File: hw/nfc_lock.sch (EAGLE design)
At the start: 2 parts, among them IC1 STM8S003F3, U1 M24SR16-YMN6T/2

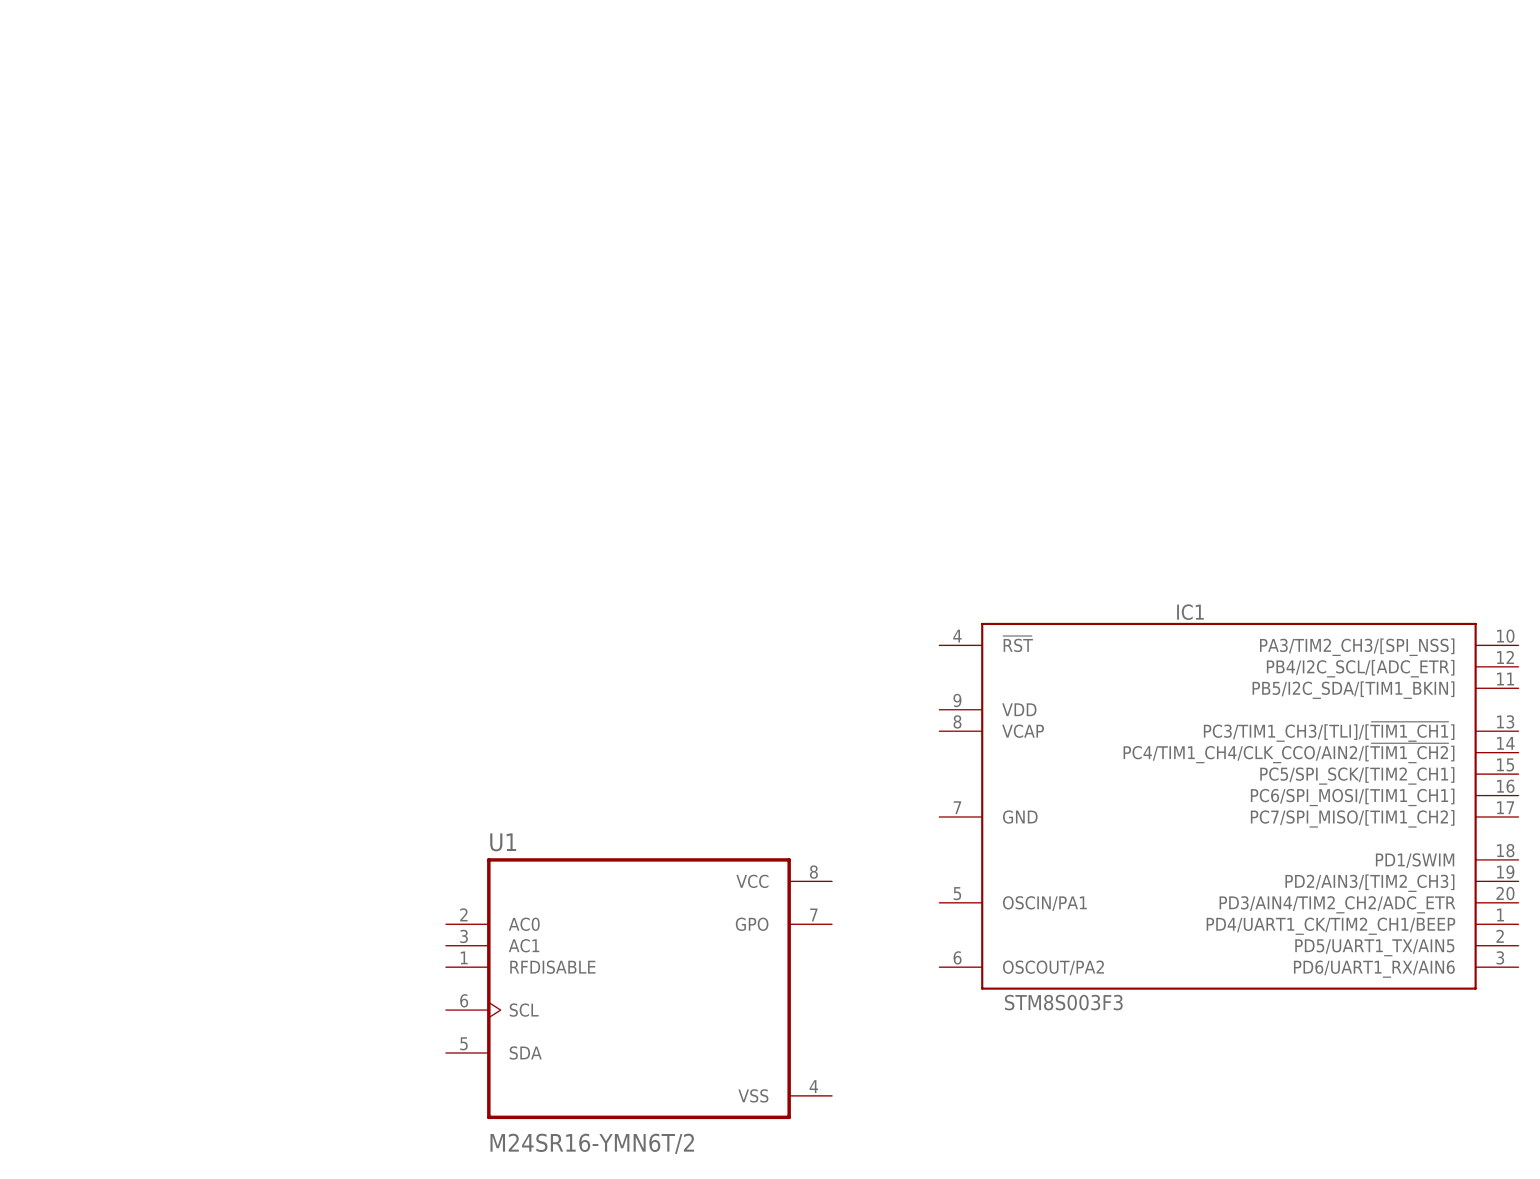
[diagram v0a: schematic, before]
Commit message: 3.3 voltage regulators + I2C lines
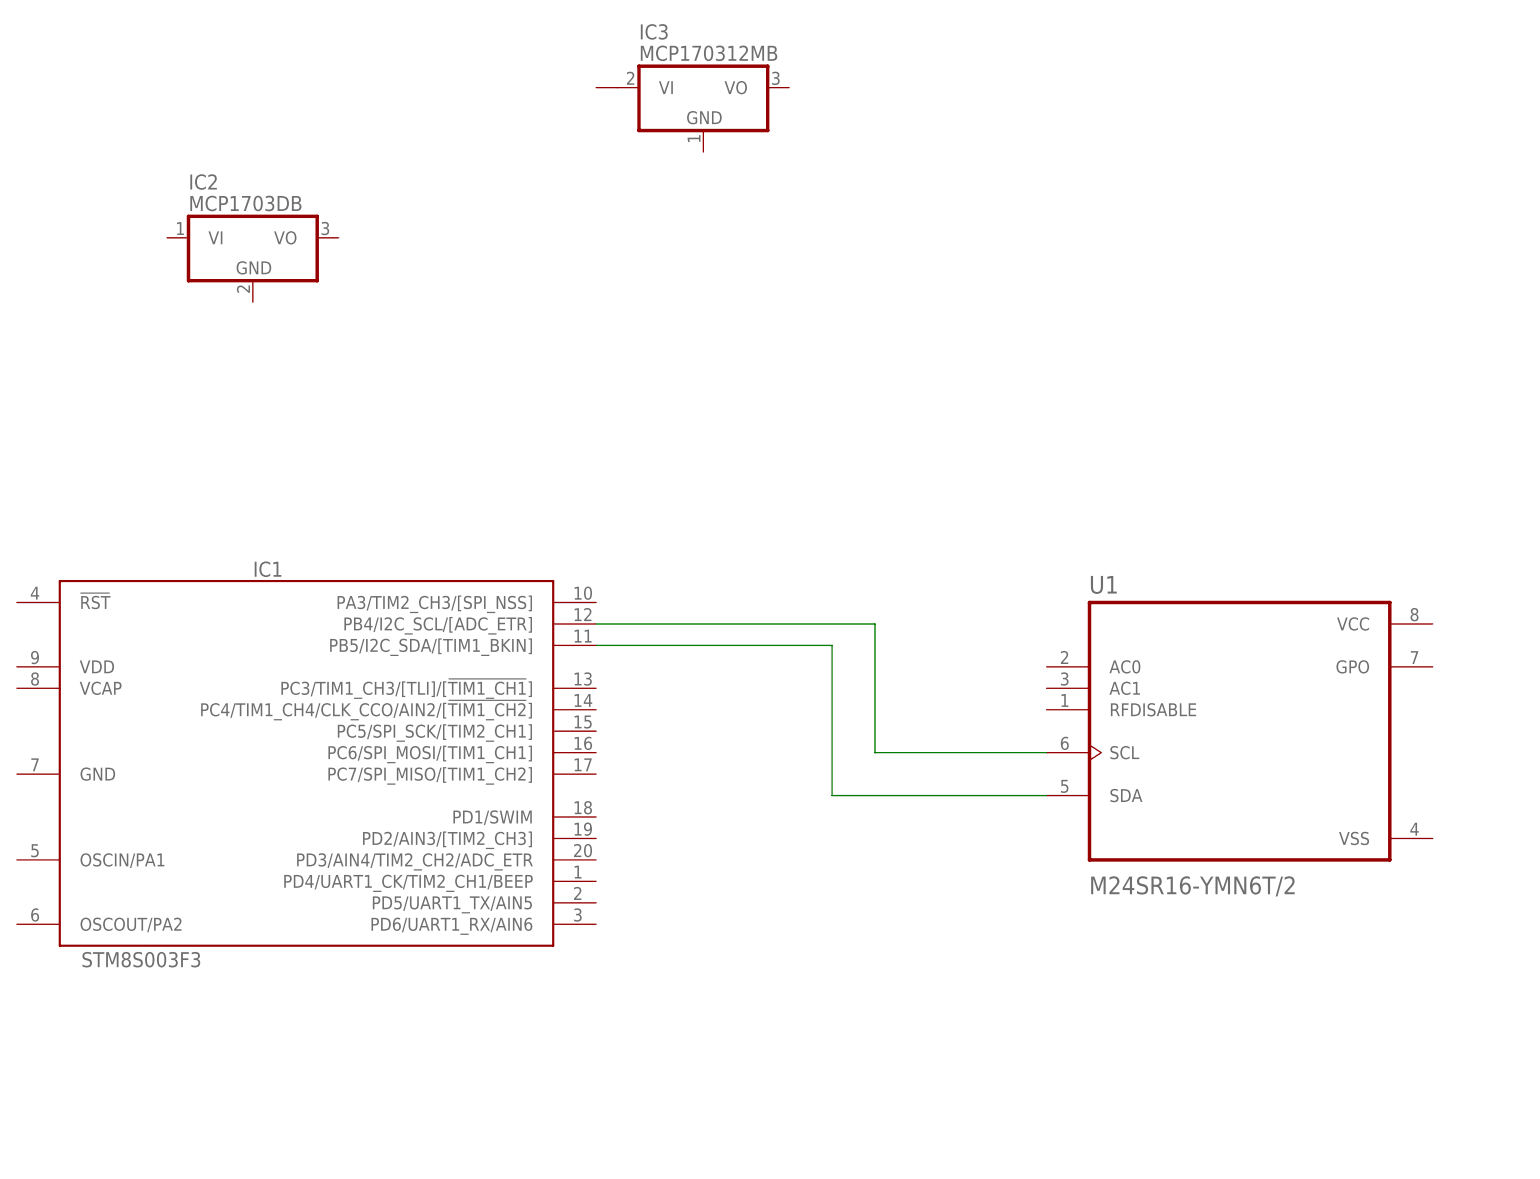
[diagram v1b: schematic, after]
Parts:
- added IC2: MCP1703DB, linear:MCP1703DB
- added IC3: MCP170312MB, linear:MCP170312MB
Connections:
- new net N$1: IC1.PB4/I2C_SCL/[ADC_ETR], U1.SCL
- new net N$2: IC1.PB5/I2C_SDA/[TIM1_BKIN], U1.SDA
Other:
- moved on the sheet: IC1, U1
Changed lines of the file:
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@@
 <part name="U1" library="m24sr16-ymn6t_2" deviceset="M24SR16-YMN6T/2" device=""/>
 <part name="IC1" library="stm8" deviceset="STM8S003" device="F3"/>
+<part name="IC2" library="linear" deviceset="MCP1703" device="DB"/>
+<part name="IC3" library="linear" deviceset="MCP1703*" device="MB" technology="12"/>
 </parts>
 <sheets>
@@
 </plain>
 <instances>
-<instance part="U1" gate="G$1" x="63.5" y="48.26"/>
-<instance part="IC1" gate="G$1" x="132.08" y="71.12"/>
+<instance part="U1" gate="G$1" x="134.62" y="78.74"/>
+<instance part="IC1" gate="G$1" x="22.86" y="76.2"/>
+<instance part="IC2" gate="G$1" x="17.78" y="137.16"/>
+<instance part="IC3" gate="G$1" x="71.12" y="154.94"/>
 </instances>
 <busses>
 </busses>
 <nets>
+<net name="N$1" class="0">
+<segment>
+<pinref part="IC1" gate="G$1" pin="PB4/I2C_SCL/[ADC_ETR]"/>
+<wire x1="58.42" y1="91.44" x2="91.44" y2="91.44" width="0.1524" layer="91"/>
+<wire x1="91.44" y1="91.44" x2="91.44" y2="76.2" width="0.1524" layer="91"/>
+<pinref part="U1" gate="G$1" pin="SCL"/>
+<wire x1="91.44" y1="76.2" x2="111.76" y2="76.2" width="0.1524" layer="91"/>
+</segment>
+</net>
+<net name="N$2" class="0">
+<segment>
+<pinref part="IC1" gate="G$1" pin="PB5/I2C_SDA/[TIM1_BKIN]"/>
+<wire x1="58.42" y1="88.9" x2="86.36" y2="88.9" width="0.1524" layer="91"/>
+<wire x1="86.36" y1="88.9" x2="86.36" y2="71.12" width="0.1524" layer="91"/>
+<pinref part="U1" gate="G$1" pin="SDA"/>
+<wire x1="86.36" y1="71.12" x2="111.76" y2="71.12" width="0.1524" layer="91"/>
+</segment>
+</net>
 </nets>
 </sheet>

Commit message: power supply circut
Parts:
- removed IC2: MCP1703DB, linear:MCP1703DB
- added C2: (no value), rcl:CPOL-EU153CLV-0405
- added C3: (no value), rcl:C-EUC1206
- added D1, D2: GF1, diode:GF1
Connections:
- new net +5V: D1.A
- new net +5V/1: C3.1, IC3.VO
- new net 0V: C2.-, C3.2, IC3.GND
- new net N$3: D1.C, D2.A
- new net N$4: C2.+, D2.C, IC3.VI1
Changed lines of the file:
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@@
 <layer number="97" name="Info" color="7" fill="1" visible="yes" active="yes"/>
 <layer number="98" name="Guide" color="6" fill="1" visible="yes" active="yes"/>
+<layer number="99" name="SpiceOrder" color="5" fill="1" visible="yes" active="yes"/>
 </layers>
 <schematic xreflabel="%F%N/%S.%C%R" xrefpart="/%S.%C%R">
@@
 <part name="U1" library="m24sr16-ymn6t_2" deviceset="M24SR16-YMN6T/2" device=""/>
 <part name="IC1" library="stm8" deviceset="STM8S003" device="F3"/>
-<part name="IC2" library="linear" deviceset="MCP1703" device="DB"/>
 <part name="IC3" library="linear" deviceset="MCP1703*" device="MB" technology="12"/>
+<part name="SUPPLY1" library="supply2" deviceset="+5V" device=""/>
+<part name="SUPPLY2" library="supply2" deviceset="+5V/1" device="" value="+3.3V"/>
+<part name="SUPPLY3" library="supply2" deviceset="0V" device=""/>
+<part name="C2" library="rcl" deviceset="CPOL-EU" device="153CLV-0405"/>
+<part name="C3" library="rcl" deviceset="C-EU" device="C1206"/>
+<part name="D1" library="diode" deviceset="GF1" device=""/>
+<part name="D2" library="diode" deviceset="GF1" device=""/>
+<part name="SUPPLY4" library="supply2" deviceset="0V" device=""/>
+<part name="SUPPLY5" library="supply2" deviceset="0V" device=""/>
 </parts>
 <sheets>
@@
 <instance part="U1" gate="G$1" x="134.62" y="78.74"/>
 <instance part="IC1" gate="G$1" x="22.86" y="76.2"/>
-<instance part="IC2" gate="G$1" x="17.78" y="137.16"/>
 <instance part="IC3" gate="G$1" x="71.12" y="154.94"/>
+<instance part="SUPPLY1" gate="+5V" x="27.94" y="157.48"/>
+<instance part="SUPPLY2" gate="G$1" x="93.98" y="157.48"/>
+<instance part="SUPPLY3" gate="0V" x="71.12" y="139.7"/>
+<instance part="C2" gate="G$1" x="53.34" y="152.4"/>
+<instance part="C3" gate="G$1" x="86.36" y="152.4"/>
+<instance part="D1" gate="D" x="35.56" y="154.94"/>
+<instance part="D2" gate="D" x="45.72" y="154.94"/>
+<instance part="SUPPLY4" gate="0V" x="86.36" y="139.7"/>
+<instance part="SUPPLY5" gate="0V" x="53.34" y="139.7"/>
 </instances>
 <busses>
@@
 </segment>
 </net>
+<net name="0V" class="0">
+<segment>
+<pinref part="IC3" gate="G$1" pin="GND"/>
+<pinref part="SUPPLY3" gate="0V" pin="0V"/>
+<wire x1="71.12" y1="142.24" x2="71.12" y2="147.32" width="0.1524" layer="91"/>
+</segment>
+<segment>
+<pinref part="C3" gate="G$1" pin="2"/>
+<pinref part="SUPPLY4" gate="0V" pin="0V"/>
+<wire x1="86.36" y1="142.24" x2="86.36" y2="147.32" width="0.1524" layer="91"/>
+</segment>
+<segment>
+<pinref part="C2" gate="G$1" pin="-"/>
+<pinref part="SUPPLY5" gate="0V" pin="0V"/>
+<wire x1="53.34" y1="142.24" x2="53.34" y2="147.32" width="0.1524" layer="91"/>
+</segment>
+</net>
+<net name="+5V/1" class="0">
+<segment>
+<pinref part="IC3" gate="G$1" pin="VO"/>
+<pinref part="SUPPLY2" gate="G$1" pin="+5V/1"/>
+<wire x1="93.98" y1="154.94" x2="86.36" y2="154.94" width="0.1524" layer="91"/>
+<pinref part="C3" gate="G$1" pin="1"/>
+<wire x1="86.36" y1="154.94" x2="81.28" y2="154.94" width="0.1524" layer="91"/>
+<junction x="86.36" y="154.94"/>
+</segment>
+</net>
+<net name="+5V" class="0">
+<segment>
+<pinref part="SUPPLY1" gate="+5V" pin="+5V"/>
+<pinref part="D1" gate="D" pin="A"/>
+<wire x1="33.02" y1="154.94" x2="27.94" y2="154.94" width="0.1524" layer="91"/>
+</segment>
+</net>
+<net name="N$3" class="0">
+<segment>
+<pinref part="D1" gate="D" pin="C"/>
+<pinref part="D2" gate="D" pin="A"/>
+<wire x1="43.18" y1="154.94" x2="38.1" y2="154.94" width="0.1524" layer="91"/>
+</segment>
+</net>
+<net name="N$4" class="0">
+<segment>
+<pinref part="IC3" gate="G$1" pin="VI1"/>
+<pinref part="D2" gate="D" pin="C"/>
+<wire x1="48.26" y1="154.94" x2="53.34" y2="154.94" width="0.1524" layer="91"/>
+<pinref part="C2" gate="G$1" pin="+"/>
+<wire x1="53.34" y1="154.94" x2="58.42" y2="154.94" width="0.1524" layer="91"/>
+<junction x="53.34" y="154.94"/>
+</segment>
+</net>

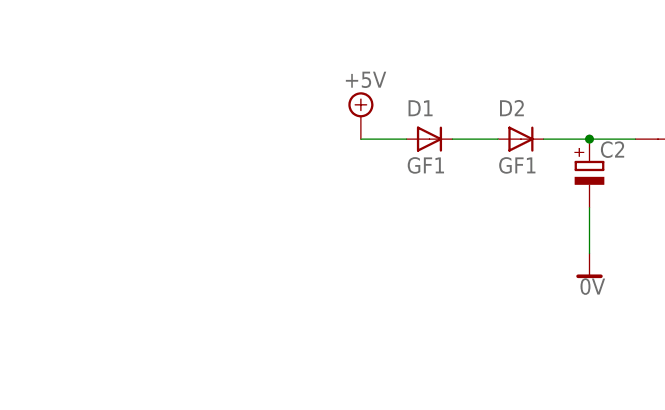
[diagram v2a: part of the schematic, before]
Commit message: power supply pads added
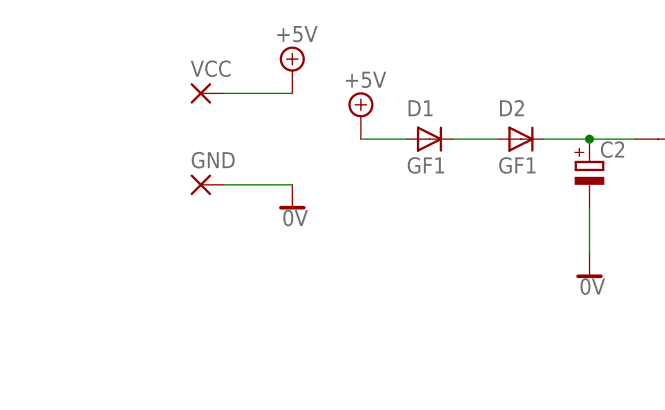
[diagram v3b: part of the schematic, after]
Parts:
- added GND, VCC: (no value), wirepad:SMD2
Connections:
- net +5V: now also VCC.P
- net 0V: now also GND.P
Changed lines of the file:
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@@
 <part name="SUPPLY4" library="supply2" deviceset="0V" device=""/>
 <part name="SUPPLY5" library="supply2" deviceset="0V" device=""/>
+<part name="VCC" library="wirepad" deviceset="SMD2" device=""/>
+<part name="GND" library="wirepad" deviceset="SMD2" device=""/>
+<part name="SUPPLY6" library="supply2" deviceset="0V" device=""/>
+<part name="SUPPLY7" library="supply2" deviceset="+5V" device=""/>
 </parts>
 <sheets>
@@
 <instance part="SUPPLY4" gate="0V" x="86.36" y="139.7"/>
 <instance part="SUPPLY5" gate="0V" x="53.34" y="139.7"/>
+<instance part="VCC" gate="1" x="10.16" y="160.02"/>
+<instance part="GND" gate="1" x="10.16" y="149.86"/>
+<instance part="SUPPLY6" gate="0V" x="20.32" y="147.32"/>
+<instance part="SUPPLY7" gate="+5V" x="20.32" y="162.56"/>
 </instances>
 <busses>
@@
 <wire x1="53.34" y1="142.24" x2="53.34" y2="147.32" width="0.1524" layer="91"/>
 </segment>
+<segment>
+<pinref part="GND" gate="1" pin="P"/>
+<pinref part="SUPPLY6" gate="0V" pin="0V"/>
+<wire x1="20.32" y1="149.86" x2="12.7" y2="149.86" width="0.1524" layer="91"/>
+</segment>
 </net>
 <net name="+5V/1" class="0">
@@
 <wire x1="33.02" y1="154.94" x2="27.94" y2="154.94" width="0.1524" layer="91"/>
 </segment>
+<segment>
+<pinref part="VCC" gate="1" pin="P"/>
+<pinref part="SUPPLY7" gate="+5V" pin="+5V"/>
+<wire x1="20.32" y1="160.02" x2="12.7" y2="160.02" width="0.1524" layer="91"/>
+</segment>
 </net>

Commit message: USB powersupply
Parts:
- removed GND, VCC: (no value), wirepad:SMD2
- added X1: MINI-USB-32005-301, con-cypressindustries:MINI-USB-32005-301
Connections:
- net +5V: now also X1.1; no longer VCC.P
- net +5V/1: now also IC1.VDD, U1.VCC
- net 0V: now also IC1.GND, U1.VSS, X1.5; no longer GND.P
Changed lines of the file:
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@@
 <part name="SUPPLY4" library="supply2" deviceset="0V" device=""/>
 <part name="SUPPLY5" library="supply2" deviceset="0V" device=""/>
-<part name="VCC" library="wirepad" deviceset="SMD2" device=""/>
-<part name="GND" library="wirepad" deviceset="SMD2" device=""/>
 <part name="SUPPLY6" library="supply2" deviceset="0V" device=""/>
 <part name="SUPPLY7" library="supply2" deviceset="+5V" device=""/>
+<part name="X1" library="con-cypressindustries" deviceset="MINI-USB-" device="32005-301"/>
+<part name="SUPPLY8" library="supply2" deviceset="+5V/1" device="" value="+3.3V"/>
+<part name="SUPPLY9" library="supply2" deviceset="0V" device=""/>
+<part name="SUPPLY10" library="supply2" deviceset="0V" device=""/>
+<part name="SUPPLY11" library="supply2" deviceset="+5V/1" device="" value="+3.3V"/>
 </parts>
 <sheets>
@@
 <instance part="SUPPLY4" gate="0V" x="86.36" y="139.7"/>
 <instance part="SUPPLY5" gate="0V" x="53.34" y="139.7"/>
-<instance part="VCC" gate="1" x="10.16" y="160.02"/>
-<instance part="GND" gate="1" x="10.16" y="149.86"/>
-<instance part="SUPPLY6" gate="0V" x="20.32" y="147.32"/>
-<instance part="SUPPLY7" gate="+5V" x="20.32" y="162.56"/>
+<instance part="SUPPLY6" gate="0V" x="12.7" y="157.48"/>
+<instance part="SUPPLY7" gate="+5V" x="17.78" y="152.4"/>
+<instance part="X1" gate="G$1" x="2.54" y="154.94" rot="R180"/>
+<instance part="SUPPLY8" gate="G$1" x="-22.86" y="88.9"/>
+<instance part="SUPPLY9" gate="0V" x="-22.86" y="71.12"/>
+<instance part="SUPPLY10" gate="0V" x="157.48" y="58.42"/>
+<instance part="SUPPLY11" gate="G$1" x="157.48" y="101.6"/>
 </instances>
 <busses>
@@
 </segment>
 <segment>
-<pinref part="GND" gate="1" pin="P"/>
+<pinref part="X1" gate="G$1" pin="5"/>
 <pinref part="SUPPLY6" gate="0V" pin="0V"/>
-<wire x1="20.32" y1="149.86" x2="12.7" y2="149.86" width="0.1524" layer="91"/>
+<wire x1="12.7" y1="160.02" x2="7.62" y2="160.02" width="0.1524" layer="91"/>
+</segment>
+<segment>
+<pinref part="IC1" gate="G$1" pin="GND"/>
+<pinref part="SUPPLY9" gate="0V" pin="0V"/>
+<wire x1="-22.86" y1="73.66" x2="-10.16" y2="73.66" width="0.1524" layer="91"/>
+</segment>
+<segment>
+<pinref part="U1" gate="G$1" pin="VSS"/>
+<pinref part="SUPPLY10" gate="0V" pin="0V"/>
+<wire x1="157.48" y1="60.96" x2="157.48" y2="66.04" width="0.1524" layer="91"/>
 </segment>
 </net>
@@
 <junction x="86.36" y="154.94"/>
 </segment>
+<segment>
+<pinref part="IC1" gate="G$1" pin="VDD"/>
+<pinref part="SUPPLY8" gate="G$1" pin="+5V/1"/>
+<wire x1="-22.86" y1="86.36" x2="-10.16" y2="86.36" width="0.1524" layer="91"/>
+</segment>
+<segment>
+<pinref part="U1" gate="G$1" pin="VCC"/>
+<pinref part="SUPPLY11" gate="G$1" pin="+5V/1"/>
+<wire x1="157.48" y1="99.06" x2="157.48" y2="91.44" width="0.1524" layer="91"/>
+</segment>
 </net>
 <net name="+5V" class="0">
@@
 </segment>
 <segment>
-<pinref part="VCC" gate="1" pin="P"/>
+<pinref part="X1" gate="G$1" pin="1"/>
 <pinref part="SUPPLY7" gate="+5V" pin="+5V"/>
-<wire x1="20.32" y1="160.02" x2="12.7" y2="160.02" width="0.1524" layer="91"/>
+<wire x1="17.78" y1="149.86" x2="7.62" y2="149.86" width="0.1524" layer="91"/>
 </segment>
 </net>
